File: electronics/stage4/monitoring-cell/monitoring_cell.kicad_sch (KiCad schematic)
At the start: 18 parts, among them J1 LAB RAILS ONLY, J2 MCU ENDPOINT/CONTROL, J3 EXTERNAL SUPERVISION, J4 CURRENT ADC INTERFACE, U1 REF3440DBVR, U2 OPA391DBVR, U3 TMUX1136DGSR

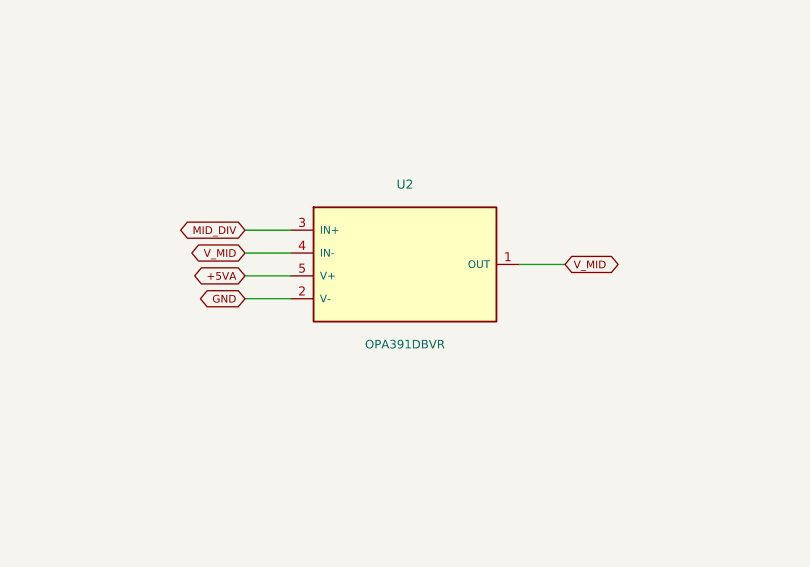
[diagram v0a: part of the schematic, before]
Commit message: Verify phase-charge study and portable source reproduction
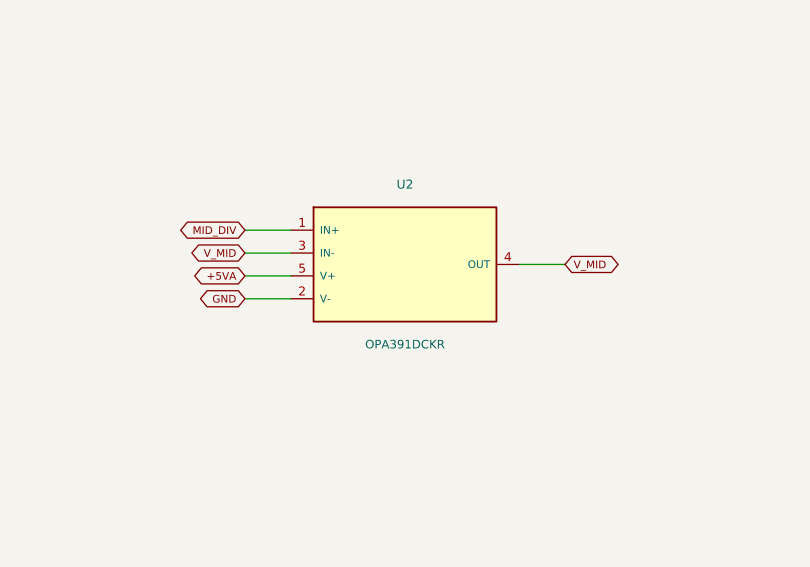
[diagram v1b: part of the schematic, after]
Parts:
- U2: value OPA391DBVR -> OPA391DCKR; footprint ato_s4:SOT-23-5 -> ato_s4:SOT-353_SC-70-5
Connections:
- net MID_DIV: now also U2.1 (IN+); no longer U2.3 (IN+)
- net V_MID: now also U2.3 (IN-); no longer U2.1 (OUT)
